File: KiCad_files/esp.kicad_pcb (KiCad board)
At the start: 2 copper layers, 86 x 75 mm, 69 parts, among them J1 Conn_01x02_Pin, J2 USB4105-GF-A, J3 Conn_01x16_Pin, Q2 DMP3099L, SW1 SLW-171175-7A-N-D, U1 B3U-1000P, U12 ESP32-S3-MINI-1U, U13 BNO085, U2 1060, U7 LTC4412xS6

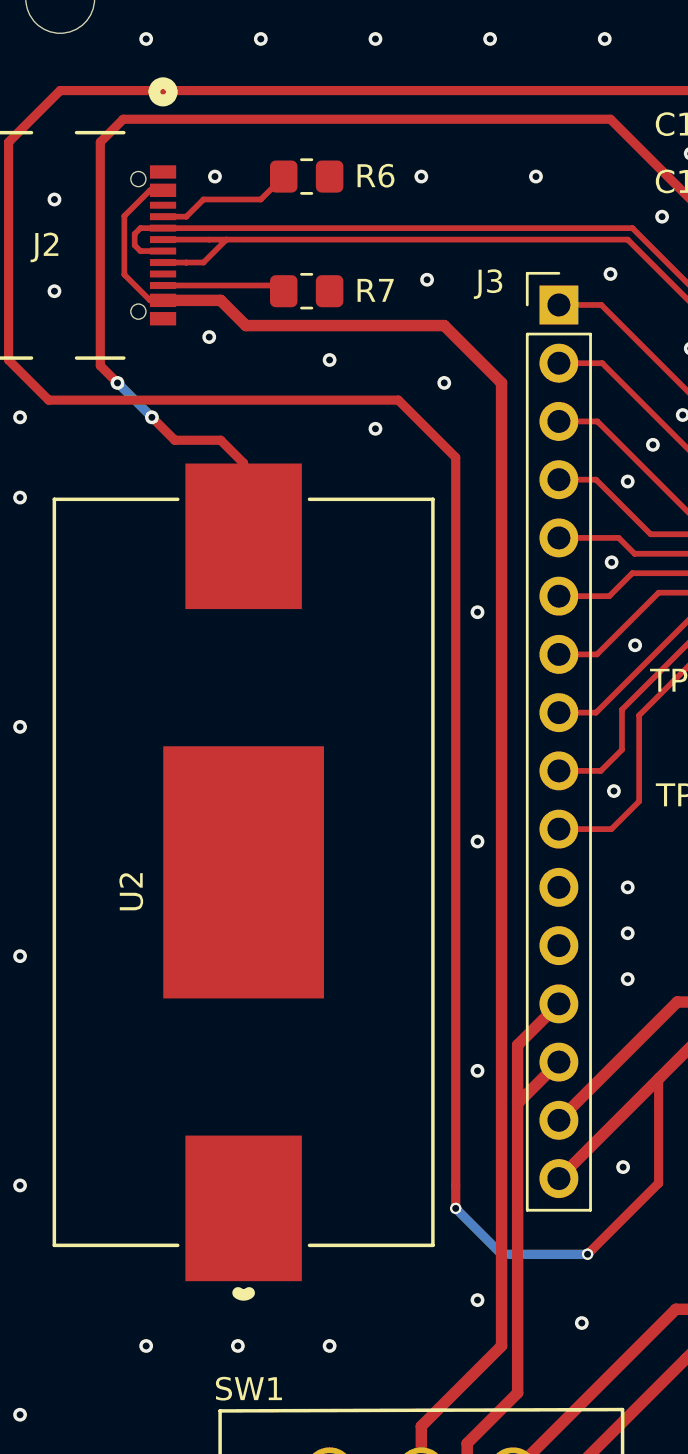
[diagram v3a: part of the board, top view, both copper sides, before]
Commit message: more vias close to USB GNDs
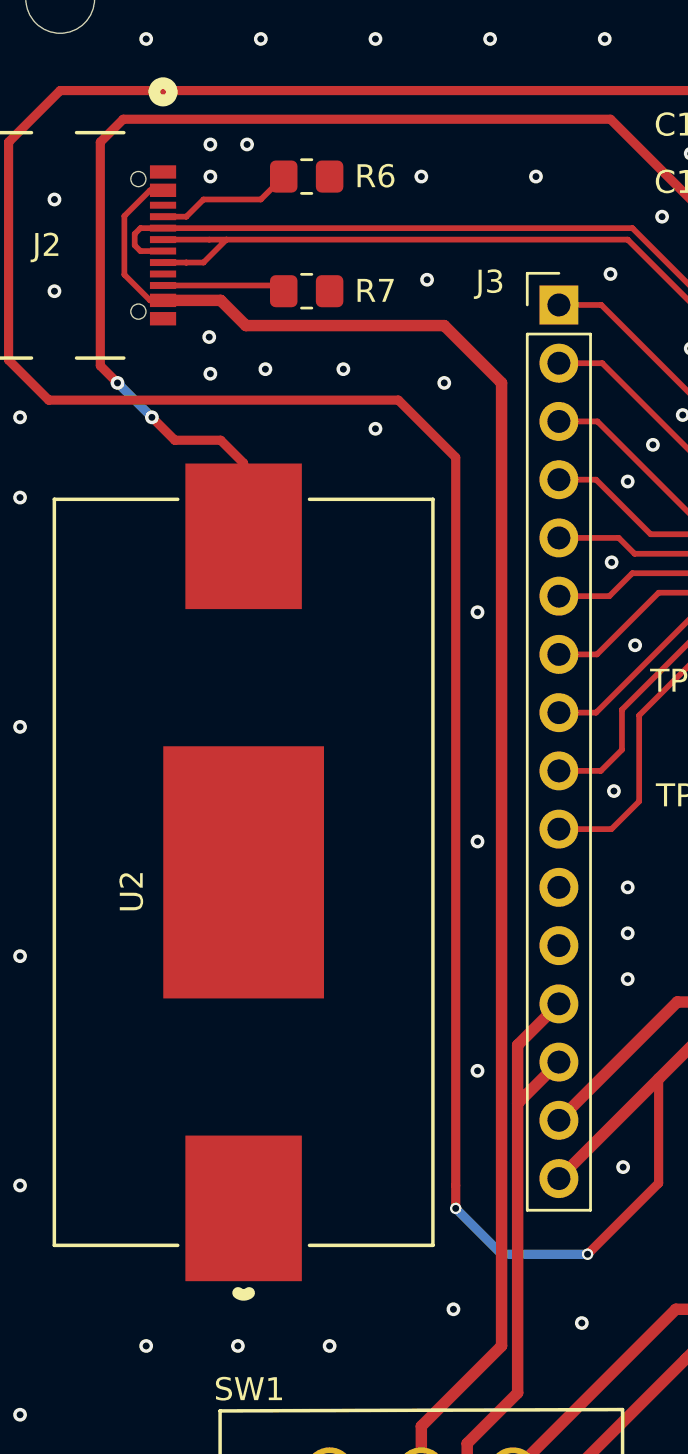
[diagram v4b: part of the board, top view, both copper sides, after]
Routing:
- net GND: vias 178 -> 182
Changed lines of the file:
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@@
+	)
+	(via
+		(at 93.4 34.6)
+		(size 0.6)
+		(drill 0.3)
+		(layers "F.Cu" "B.Cu")
+		(free yes)
+		(net 1)
 	)
 	(via
@@
 	)
 	(via
+		(at 91.8 44.6)
+		(size 0.6)
+		(drill 0.3)
+		(layers "F.Cu" "B.Cu")
+		(free yes)
+		(net 1)
+	)
+	(via
 		(at 161 30)
 		(size 0.6)
@@
 	)
 	(via
-		(at 92 36)
+		(at 91.8 36)
 		(size 0.6)
 		(drill 0.3)
@@
 	)
 	(via
+		(at 94.2 44.4)
+		(size 0.6)
+		(drill 0.3)
+		(layers "F.Cu" "B.Cu")
+		(free yes)
+		(net 1)
+	)
+	(via
 		(at 93 87)
 		(size 0.6)
@@
 	)
 	(via
-		(at 97 44)
-		(size 0.6)
-		(drill 0.3)
-		(layers "F.Cu" "B.Cu")
-		(free yes)
-		(net 1)
-	)
-	(via
-		(at 103.45 85)
-		(size 0.6)
-		(drill 0.3)
+		(at 91.8 34.6)
+		(size 0.6)
+		(drill 0.3)
+		(layers "F.Cu" "B.Cu")
+		(free yes)
+		(net 1)
+	)
+	(via
+		(at 97.6 44.4)
+		(size 0.6)
+		(drill 0.3)
+		(layers "F.Cu" "B.Cu")
+		(free yes)
+		(net 1)
+	)
+	(via
+		(at 102.4 85.4)
+		(size 0.6)
+		(drill 0.3)

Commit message: changed voltage regulator footprint
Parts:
- U8: footprint Package_TO_SOT_SMD:TSOT-23-8 -> Package_TO_SOT_SMD:TSOT-23-8_HandSoldering
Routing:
- net Net-(D2-K): track 31.3 -> 33.4 mm
- net Net-(U8-EN/SYNC): track 5.15 -> 5.79 mm
- net Net-(D3-A): track 11.1 -> 11.8 mm
